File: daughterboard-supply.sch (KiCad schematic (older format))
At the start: 12 parts, among them J4 43045-1013, U15 AP62301WU-7

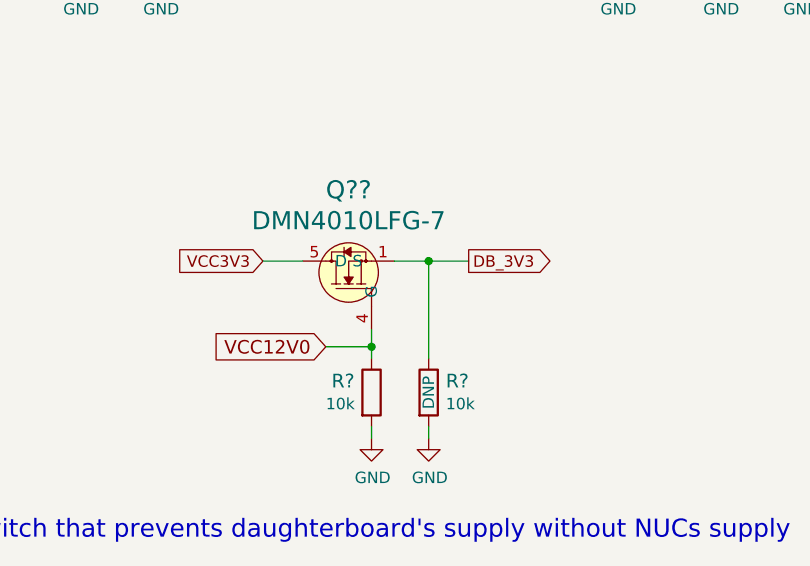
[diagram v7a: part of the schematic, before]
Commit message: FTDI layout redesign
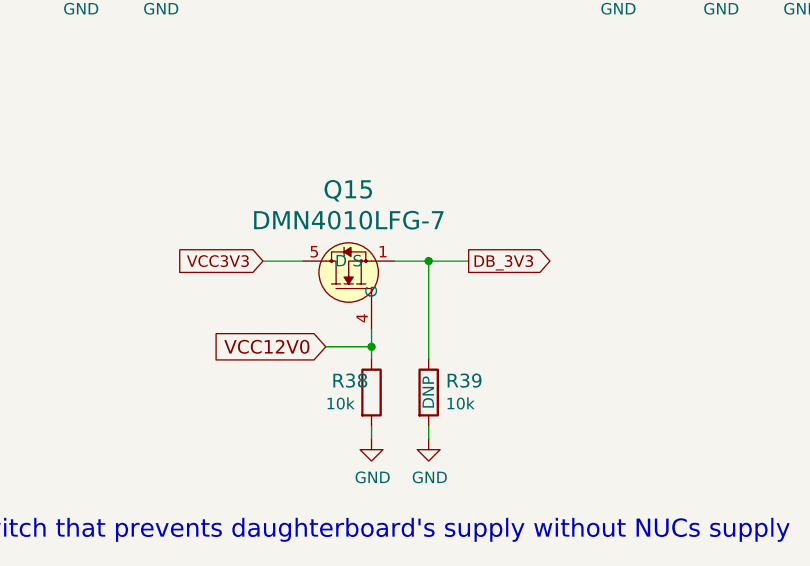
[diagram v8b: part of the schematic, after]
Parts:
- gave numbers to parts that had none: 3
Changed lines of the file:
@@
 DB_3V3
 $Comp
-L antmicroTransistorsFETsMOSFETsSingle:DMN4010LFG-7 Q??
+L antmicroTransistorsFETsMOSFETsSingle:DMN4010LFG-7 Q15
 U 1 1 626C5C42
 P 3525 3950
-F 0 "Q??" V 3861 3950 79  0000 C CNN
+F 0 "Q15" V 3861 3950 79  0000 C CNN
 F 1 "DMN4010LFG-7" V 3726 3950 79  0000 C CNN
 F 2 "antmicro-footprints:POWERVDFN-8" H 3525 3950 79  0001 C CNN
@@
 P 3625 4700
 AR Path="/62220F27/626D67BF" Ref="#PWR?"  Part="1"
-AR Path="/623923F9/626D67BF" Ref="#PWR?"  Part="1"
-F 0 "#PWR?" H 3625 4450 50  0001 C CNN
+AR Path="/623923F9/626D67BF" Ref="#PWR0103"  Part="1"
+F 0 "#PWR0103" H 3625 4450 50  0001 C CNN
 F 1 "GND" H 3630 4527 50  0000 C CNN
 F 2 "" H 3625 4700 50  0001 C CNN
@@
 $EndComp
 $Comp
-L antmicroResistors0402:R_10k_0402 R?
+L antmicroResistors0402:R_10k_0402 R38
 U 1 1 626D757A
 P 3625 4500
-F 0 "R?" V 3575 4325 60  0000 L CNN
+F 0 "R38" V 3575 4325 60  0000 L CNN
 F 1 "R_10k_0402" H 3625 4350 60  0001 C CNN
 F 2 "antmicro-footprints:0402-res" H 3825 4700 60  0001 L CNN
@@
 P 3875 4700
 AR Path="/62220F27/626DA518" Ref="#PWR?"  Part="1"
-AR Path="/623923F9/626DA518" Ref="#PWR?"  Part="1"
-F 0 "#PWR?" H 3875 4450 50  0001 C CNN
+AR Path="/623923F9/626DA518" Ref="#PWR0104"  Part="1"
+F 0 "#PWR0104" H 3875 4450 50  0001 C CNN
 F 1 "GND" H 3880 4527 50  0000 C CNN
 F 2 "" H 3875 4700 50  0001 C CNN
@@
 	3875 3925 4050 3925
 $Comp
-L antmicroResistors0402:R_10k_0402 R?
+L antmicroResistors0402:R_10k_0402 R39
 U 1 1 626D93ED
 P 3875 4500
-F 0 "R?" V 3825 4575 60  0000 L CNN
+F 0 "R39" V 3825 4575 60  0000 L CNN
 F 1 "R_10k_0402" H 3875 4350 60  0001 C CNN
 F 2 "antmicro-footprints:0402-res" H 4075 4700 60  0001 L CNN
